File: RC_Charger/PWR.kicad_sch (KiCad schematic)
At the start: 49 parts, among them Q10 IRFH5210, Q7 IRFH5210, Q8 IRFH5210, Q9 IRFH5210, U10 MP2984, U11 INA180A1

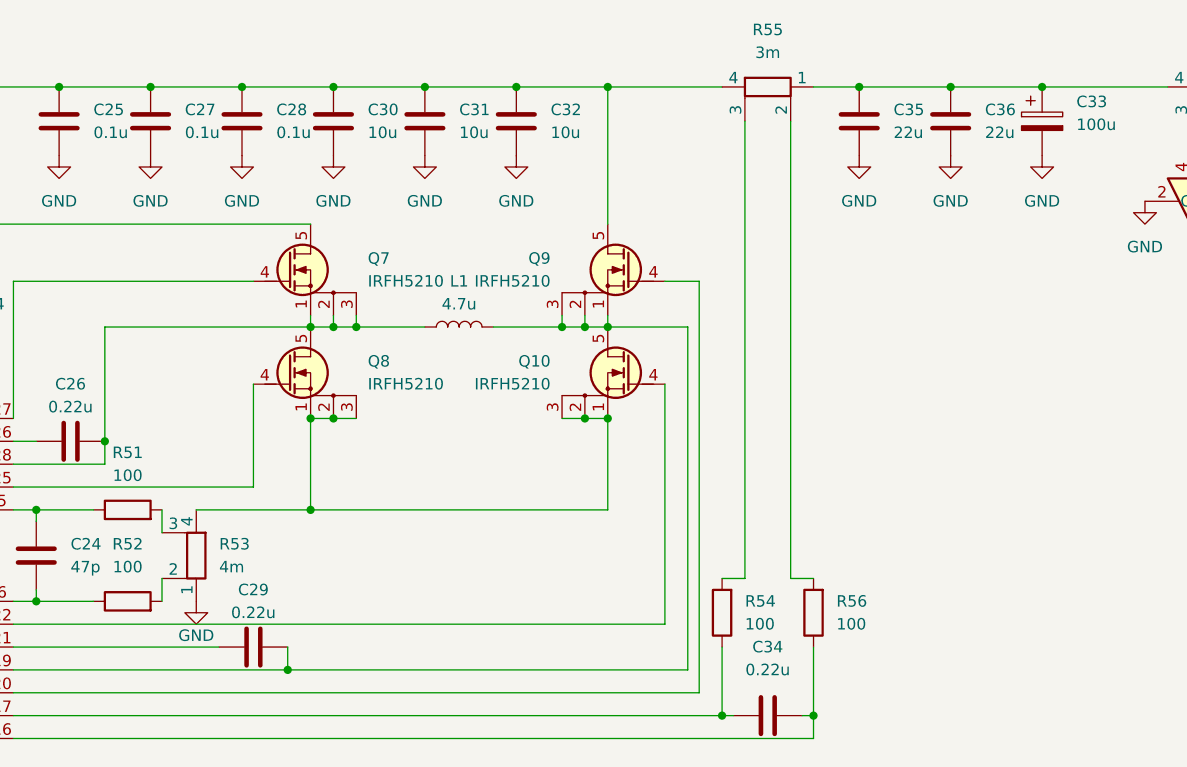
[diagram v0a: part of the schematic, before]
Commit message: Add full bom and final pcb design
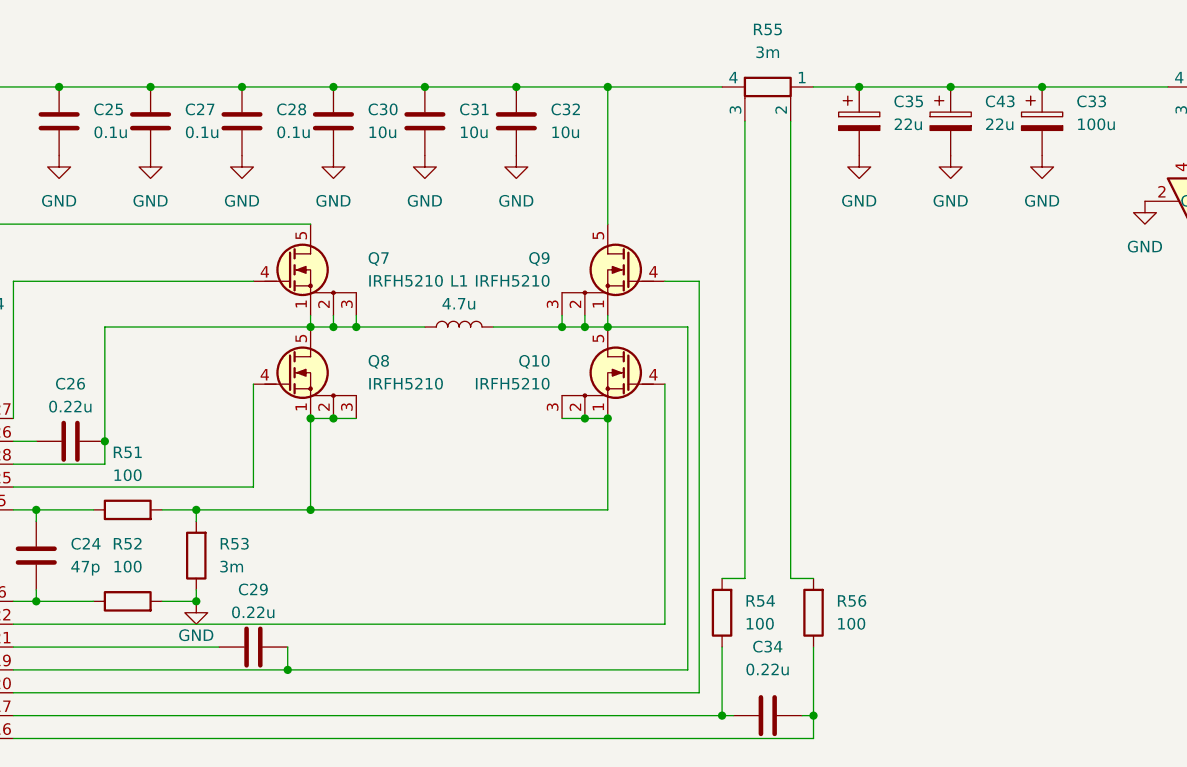
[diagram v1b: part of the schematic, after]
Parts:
- removed C35, C36: 22u, Capacitor_SMD:C_2220_5650Metric, symbol Device:C
- removed R53: 4m, Samacsys:WSLP27265L000FEA, symbol Device:R_Shunt
- added C35, C43: 22u, Capacitor_SMD:CP_Elec_6.3x5.4, symbol Device:C_Polarized
- added R53: 3m, Personal:R_Shunt_1575, symbol Device:R
- C10, C33: footprint Capacitor_SMD:CP_Elec_10x10 -> Capacitor_SMD:CP_Elec_6.3x7.7
- C11, C12, C13, C14, C30, C31, C32: footprint Capacitor_SMD:C_1210_3225Metric -> Capacitor_SMD:C_1206_3216Metric
- R55, R57: footprint Samacsys:WSLP27265L000FEA -> Resistor_SMD:R_Shunt_Vishay_WSK2512_6332Metric_T2.21mm
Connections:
- net GND: now also R52.2, C35.2, C43.2, R53.1
- net at C33.1, R55.1, R57.4: now also C35.1, C43.1
- net at Q10.1 (S), Q10.2 (S), Q10.3 (S)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: now also R51.2, R53.2
